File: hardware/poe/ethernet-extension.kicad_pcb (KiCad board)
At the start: 4 copper layers, 40 x 40 mm, 121 parts, among them J1 STACK-UP-HIGH, J2 STACK-DOWN, J3 STACK-UP-HIGH, J4 STACK-DOWN, P1 RJPSL-001TA1, P2 CONN_1, Q1 2N7002P, Q2 MMBTA42, Q3 FDC2512, T1 EFD15, U1 W5500, U2 M24C64, U3 LTC4267D, U4 PS2911-1, U5 DRILL, U6 DRILL, U7 DRILL, U8 DRILL, X1 25Mhz

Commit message: Add 3d information (tbc)
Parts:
- C1, C10, C11, C12, C14, C16, C17, C18, C19, C20, C21, C22, C23, C24, C3, C38, C39, C5, C6, C8, C9, L1, L2: footprint 0603 -> kicad-libraries:C0603
- C13: footprint 0805P -> kicad-libraries:0805P
- C15: footprint 3528-21 -> kicad-libraries:3528-21
- C2, C4: footprint 0805P -> kicad-libraries:C0805P
- C25, C26, C29, C30, C31, C32, C33, C37, C40, C41, C42: footprint 1206 -> kicad-libraries:C1206
- C28, C34, C35, C36, C7: footprint 0805 -> kicad-libraries:C0805
- D1, D2: footprint MiniDIP -> kicad-libraries:MiniDIP
- D10, D12: footprint SOD-128 -> kicad-libraries:SOD-128
- D11: footprint D0603 -> kicad-libraries:D0603
- D3: footprint DO-214AC -> kicad-libraries:DO-214AC
- D4, D5, D6, D7, D8: footprint SOD-123 -> kicad-libraries:SOD-123
- D9, Q2: footprint SOT23-3 -> kicad-libraries:SOT23-3
- FILTER1: footprint DFN16-33x135 -> kicad-libraries:DFN16-33x135
- Fiducial_Mark (x7): footprint Fiducial_Mark -> kicad-libraries:Fiducial_Mark
- G***: footprint Logo_31x31 -> kicad-libraries:Logo_31x31
- J1, J3: footprint BTB08-ACS-TOP -> kicad-libraries:BTB08-ACS-TOP
- J2, J4: footprint BTB08-ACS-BTM -> kicad-libraries:BTB08-ACS-BTM
- L5, L6: footprint NR4040 -> kicad-libraries:NR4040
- P1: footprint RJPSL-001TA1 -> kicad-libraries:RJPSL-001TA1
- P2: footprint con -> kicad-libraries:con
- Q1: footprint SOT23GDS -> kicad-libraries:SOT23GDS
- Q3: footprint SuperSOT6 -> kicad-libraries:SuperSOT6
- R1, R10, R11, R12, R13, R14, R15, R16, R17, R18, R19, R2, R20, R21, R22, R25, R26, R27, R28, R29, R3, R30, R31, R32, R33, R4, R5, R6, R7, R8, R9: footprint 0603 -> kicad-libraries:R0603
- R23: footprint 1210 -> kicad-libraries:R1210
- R24: footprint 0603 -> kicad-libraries:0603
- RP3: footprint 4X0603 -> kicad-libraries:4X0603
- T1: footprint EFD15 -> kicad-libraries:EFD15
- U1: footprint LQFP48 -> kicad-libraries:LQFP48
- U2: footprint SOIC8 -> kicad-libraries:SOIC8
- U3: footprint DFN16_5x3 -> kicad-libraries:DFN16_5x3
- U4: footprint PS2911 -> kicad-libraries:PS2911
- U5, U6, U7, U8: footprint DRILL_NP -> kicad-libraries:DRILL_NP
- VAL: footprint CE_5mm -> kicad-libraries:CE_5mm
- VAL: footprint WEEE_7mm -> kicad-libraries:WEEE_7mm
- X1: footprint CRYSTAL_3225 -> kicad-libraries:CRYSTAL_3225
- turned VAL to 180 degrees
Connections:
- FILTER1 pad 10: (no net) -> Net-(FILTER1-Pad10)
- FILTER1 pad 7: (no net) -> Net-(FILTER1-Pad7)
- FILTER1 pad 8: (no net) -> Net-(FILTER1-Pad8)
- FILTER1 pad 9: (no net) -> Net-(FILTER1-Pad9)
- J1 pad 25: (no net) -> Net-(J1-Pad25)
- J1 pad 27: (no net) -> Net-(J1-Pad27)
- J1 pad 29: (no net) -> Net-(J1-Pad29)
- J2 pad 23: (no net) -> Net-(J2-Pad23)
- T1 pad 1: (no net) -> Net-(T1-Pad1)
- T1 pad 3: (no net) -> Net-(T1-Pad3)
- U1 pad 12: (no net) -> Net-(U1-Pad12)
- U1 pad 13: (no net) -> Net-(U1-Pad13)
- U1 pad 18: (no net) -> Net-(U1-Pad18)
- U1 pad 24: (no net) -> Net-(U1-Pad24)
- U1 pad 26: (no net) -> Net-(U1-Pad26)
- U1 pad 27: (no net) -> Net-(U1-Pad27)
- U1 pad 46: (no net) -> Net-(U1-Pad46)
- U1 pad 47: (no net) -> Net-(U1-Pad47)
- U1 pad 7: (no net) -> Net-(U1-Pad7)
- U2 pad 7: (no net) -> Net-(U2-Pad7)
- U3 pad 6: (no net) -> Net-(U3-Pad6)
- U3 pad 8: (no net) -> Net-(U3-Pad8)
- U3 pad 9: (no net) -> Net-(U3-Pad9)

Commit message: Add 3d information (tbc)
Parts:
- C1, C10, C11, C12, C14, C16, C17, C18, C19, C20, C21, C22, C23, C24, C3, C38, C39, C5, C6, C8, C9, L1, L2: footprint kicad-libraries:C0603 -> C0603
- C13: footprint kicad-libraries:0805P -> 0805P
- C15: footprint kicad-libraries:3528-21 -> 3528-21
- C2, C4: footprint kicad-libraries:C0805P -> C0805P
- C25, C26, C29, C30, C31, C32, C33, C37, C40, C41, C42: footprint kicad-libraries:C1206 -> C1206
- C28, C34, C35, C36, C7: footprint kicad-libraries:C0805 -> C0805
- D10, D12: footprint kicad-libraries:SOD-128 -> SOD-128
- D11: footprint kicad-libraries:D0603 -> D0603
- D3: footprint kicad-libraries:DO-214AC -> DO-214AC
- D4, D5, D6, D7, D8: footprint kicad-libraries:SOD-123 -> SOD-123
- D9, Q2: footprint kicad-libraries:SOT23-3 -> SOT23-3
- FILTER1: footprint kicad-libraries:DFN16-33x135 -> DFN16-33x135
- J1, J3: footprint kicad-libraries:BTB08-ACS-TOP -> BTB08-ACS-TOP
- J2, J4: footprint kicad-libraries:BTB08-ACS-BTM -> BTB08-ACS-BTM
- L5, L6: footprint kicad-libraries:NR4040 -> NR4040
- P1: footprint kicad-libraries:RJPSL-001TA1 -> RJPSL-001TA1
- P2: footprint kicad-libraries:con -> con
- Q1: footprint kicad-libraries:SOT23GDS -> SOT23GDS
- Q3: footprint kicad-libraries:SuperSOT6 -> SuperSOT6
- R1, R10, R11, R12, R13, R14, R15, R16, R17, R18, R19, R2, R20, R21, R22, R25, R26, R27, R28, R29, R3, R30, R31, R32, R33, R4, R5, R6, R7, R8, R9: footprint kicad-libraries:R0603 -> R0603
- R23: footprint kicad-libraries:R1210 -> R1210
- R24: footprint kicad-libraries:0603 -> R0603
- RP3: footprint kicad-libraries:4X0603 -> 4X0603
- T1: footprint kicad-libraries:EFD15 -> EFD15
- U1: footprint kicad-libraries:LQFP48 -> LQFP48
- U2: footprint kicad-libraries:SOIC8 -> SOIC8
- U3: footprint kicad-libraries:DFN16_5x3 -> DFN16_5x3
- U4: footprint kicad-libraries:PS2911 -> PS2911
- U5, U6, U7, U8: footprint kicad-libraries:DRILL_NP -> DRILL_NP
- X1: footprint kicad-libraries:CRYSTAL_3225 -> CRYSTAL_3225

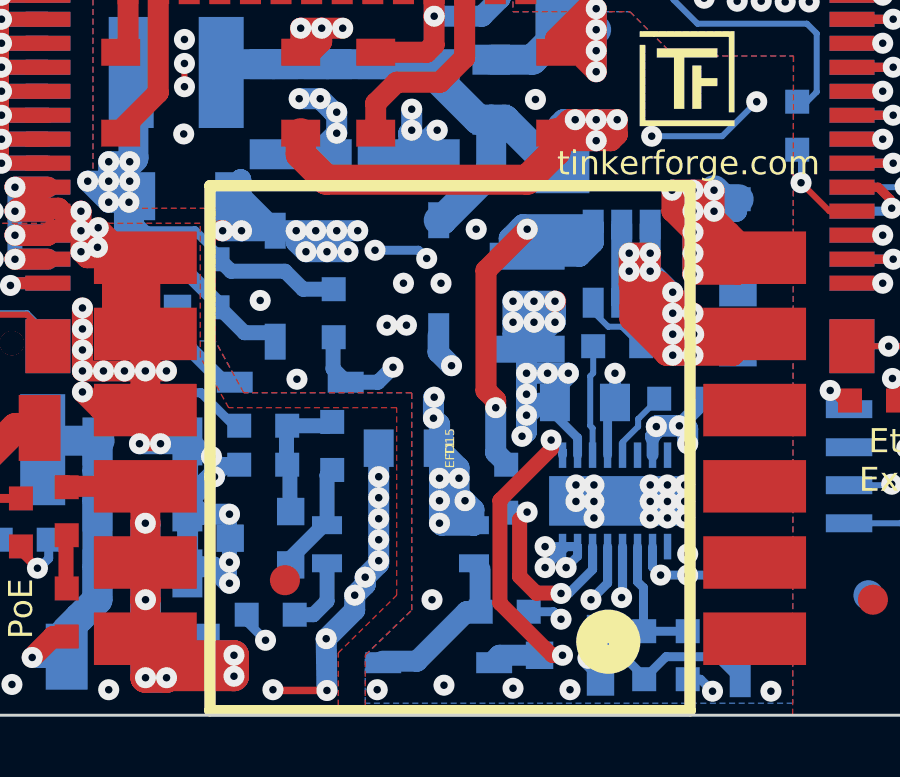
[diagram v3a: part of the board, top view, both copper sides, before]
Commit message: Add 3d model (*.step & *.FCStd)
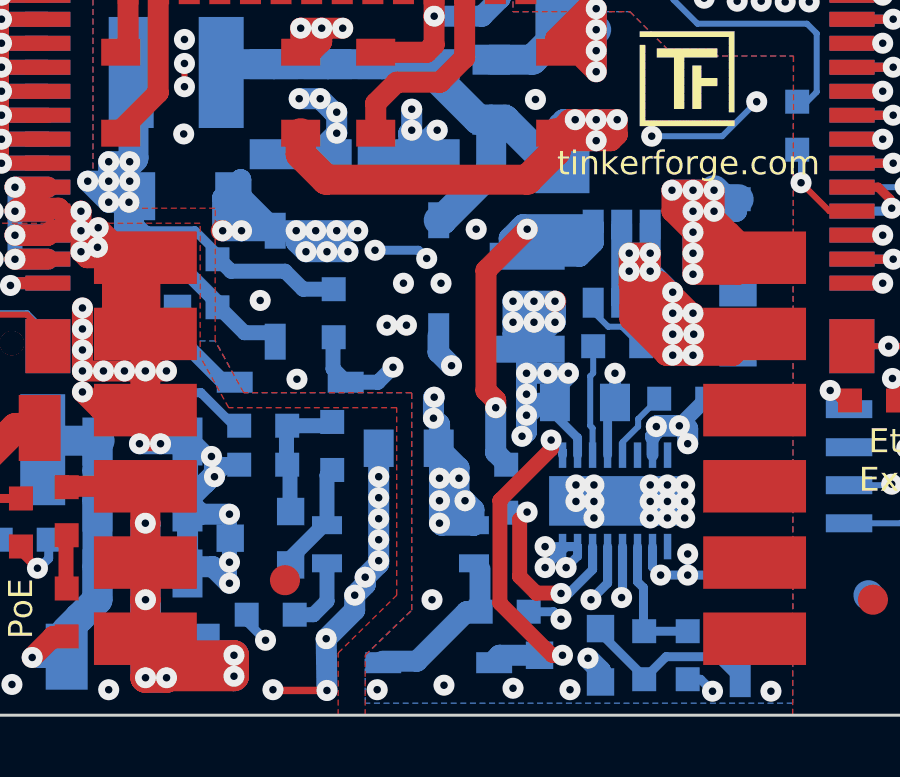
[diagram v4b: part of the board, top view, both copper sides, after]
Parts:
- T1: footprint EFD15 -> kicad-libraries:EFD15
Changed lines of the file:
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@@
     (pad 2 smd rect (at 0.8001 0 270) (size 0.8001 0.8001) (layers Vorderseite F.Paste F.Mask)
       (net 48 "Net-(D11-Pad2)"))
-    (model LED_SMD/D_0603_blue.wrl
+    (model LED_SMD/D_0603_green.wrl
       (at (xyz 0 0 0))
       (scale (xyz 1 1 1))
@@
     )
   )
-  (module EFD15 (layer Vorderseite)
-    (at 151.07666 120.05056 90)
-    (fp_text reference T1 (at 0 0 90) (layer F.SilkS)
-      (effects (font (size 0.29972 0.29972) (thickness 0.0762)))
-    )
-    (fp_text value EFD15 (at 0 0 90) (layer F.SilkS)
-      (effects (font (size 0.29972 0.29972) (thickness 0.0762)))
-    )
-    (fp_circle (center -6.52526 5.27558) (end -6.3754 5.30098) (layer F.SilkS) (width 0.381))
-    (fp_circle (center -6.49986 5.25018) (end -6.12394 5.37464) (layer F.SilkS) (width 0.381))
-    (fp_circle (center -6.47446 5.27558) (end -5.84962 5.42544) (layer F.SilkS) (width 0.381))
-    (fp_circle (center -6.44906 5.27558) (end -5.72516 5.77596) (layer F.SilkS) (width 0.381))
-    (fp_line (start -8.7503 8.001) (end 8.7503 8.001) (layer F.SilkS) (width 0.381))
-    (fp_line (start 8.7503 8.001) (end 8.7503 -8.001) (layer F.SilkS) (width 0.381))
-    (fp_line (start 8.7503 -8.001) (end -8.7503 -8.001) (layer F.SilkS) (width 0.381))
-    (fp_line (start -8.7503 -8.001) (end -8.7503 8.001) (layer F.SilkS) (width 0.381))
-    (pad 1 smd rect (at -6.35 10.15492 90) (size 1.75006 3.429) (layers Vorderseite F.Paste F.Mask)
-      (net 114 "Net-(T1-Pad1)"))
-    (pad 2 smd rect (at -3.81 10.15492 90) (size 1.75006 3.429) (layers Vorderseite F.Paste F.Mask))
-    (pad 3 smd rect (at -1.27 10.15492 90) (size 1.75006 3.429) (layers Vorderseite F.Paste F.Mask)
-      (net 115 "Net-(T1-Pad3)"))
-    (pad 4 smd rect (at 1.27 10.15492 90) (size 1.75006 3.429) (layers Vorderseite F.Paste F.Mask))
-    (pad 5 smd rect (at 3.81 10.15492 90) (size 1.75006 3.429) (layers Vorderseite F.Paste F.Mask)
-      (net 34 "Net-(C35-Pad1)"))
-    (pad 6 smd rect (at 6.35 10.15492 90) (size 1.75006 3.429) (layers Vorderseite F.Paste F.Mask)
-      (net 33 "Net-(C33-Pad2)"))
-    (pad 7 smd rect (at 6.35 -10.15492 90) (size 1.75006 3.429) (layers Vorderseite F.Paste F.Mask)
-      (net 7 GND))
-    (pad 8 smd rect (at 3.81 -10.15492 90) (size 1.75006 3.429) (layers Vorderseite F.Paste F.Mask)
-      (net 7 GND))
-    (pad 9 smd rect (at 1.27 -10.15492 90) (size 1.75006 3.429) (layers Vorderseite F.Paste F.Mask)
-      (net 7 GND))
-    (pad 10 smd rect (at -1.27 -10.15492 90) (size 1.75006 3.429) (layers Vorderseite F.Paste F.Mask)
-      (net 47 "Net-(D10-Pad1)"))
-    (pad 11 smd rect (at -3.81 -10.15492 90) (size 1.75006 3.429) (layers Vorderseite F.Paste F.Mask)
-      (net 47 "Net-(D10-Pad1)"))
-    (pad 12 smd rect (at -6.35 -10.15492 90) (size 1.75006 3.429) (layers Vorderseite F.Paste F.Mask)
-      (net 47 "Net-(D10-Pad1)"))
-  )
   (module LQFP48 (layer Rückseite)
     (at 160.4 96.5 90)
@@
     )
   )
+  (module kicad-libraries:EFD15 (layer Vorderseite)
+    (at 151.07666 120.05056 90)
+    (fp_text reference T1 (at -0.02 -0.46 90) (layer F.Fab)
+      (effects (font (size 0.29972 0.29972) (thickness 0.07493)))
+    )
+    (fp_text value EFD15 (at 0 0 90) (layer F.Fab)
+      (effects (font (size 0.29972 0.29972) (thickness 0.07493)))
+    )
+    (fp_circle (center -6.52526 5.27558) (end -6.3754 5.30098) (layer F.Fab) (width 0.381))
+    (fp_circle (center -6.49986 5.25018) (end -6.12394 5.37464) (layer F.Fab) (width 0.381))
+    (fp_circle (center -6.47446 5.27558) (end -5.84962 5.42544) (layer F.Fab) (width 0.381))
+    (fp_circle (center -6.44906 5.27558) (end -5.72516 5.77596) (layer F.Fab) (width 0.381))
+    (fp_line (start -8.7503 8.001) (end 8.7503 8.001) (layer F.Fab) (width 0.381))
+    (fp_line (start 8.7503 8.001) (end 8.7503 -8.001) (layer F.Fab) (width 0.381))
+    (fp_line (start 8.7503 -8.001) (end -8.7503 -8.001) (layer F.Fab) (width 0.381))
+    (fp_line (start -8.7503 -8.001) (end -8.7503 8.001) (layer F.Fab) (width 0.381))
+    (pad 1 smd rect (at -6.35 10.15492 90) (size 1.75006 3.429) (layers Vorderseite F.Paste F.Mask)
+      (net 114 "Net-(T1-Pad1)"))
+    (pad 2 smd rect (at -3.81 10.15492 90) (size 1.75006 3.429) (layers Vorderseite F.Paste F.Mask))
+    (pad 3 smd rect (at -1.27 10.15492 90) (size 1.75006 3.429) (layers Vorderseite F.Paste F.Mask)
+      (net 115 "Net-(T1-Pad3)"))
+    (pad 4 smd rect (at 1.27 10.15492 90) (size 1.75006 3.429) (layers Vorderseite F.Paste F.Mask))
+    (pad 5 smd rect (at 3.81 10.15492 90) (size 1.75006 3.429) (layers Vorderseite F.Paste F.Mask)
+      (net 34 "Net-(C35-Pad1)"))
+    (pad 6 smd rect (at 6.35 10.15492 90) (size 1.75006 3.429) (layers Vorderseite F.Paste F.Mask)
+      (net 33 "Net-(C33-Pad2)"))
+    (pad 7 smd rect (at 6.35 -10.15492 90) (size 1.75006 3.429) (layers Vorderseite F.Paste F.Mask)
+      (net 7 GND))
+    (pad 8 smd rect (at 3.81 -10.15492 90) (size 1.75006 3.429) (layers Vorderseite F.Paste F.Mask)
+      (net 7 GND))
+    (pad 9 smd rect (at 1.27 -10.15492 90) (size 1.75006 3.429) (layers Vorderseite F.Paste F.Mask)
+      (net 7 GND))
+    (pad 10 smd rect (at -1.27 -10.15492 90) (size 1.75006 3.429) (layers Vorderseite F.Paste F.Mask)
+      (net 47 "Net-(D10-Pad1)"))
+    (pad 11 smd rect (at -3.81 -10.15492 90) (size 1.75006 3.429) (layers Vorderseite F.Paste F.Mask)
+      (net 47 "Net-(D10-Pad1)"))
+    (pad 12 smd rect (at -6.35 -10.15492 90) (size 1.75006 3.429) (layers Vorderseite F.Paste F.Mask)
+      (net 47 "Net-(D10-Pad1)"))
+    (model unsorted/EFD15.wrl
+      (at (xyz 0 0 0))
+      (scale (xyz 1 1 1))
+      (rotate (xyz 0 0 -90))
+    )
+  )
